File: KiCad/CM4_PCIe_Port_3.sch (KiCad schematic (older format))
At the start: 1 part, among them J15 10018783-10113TLF

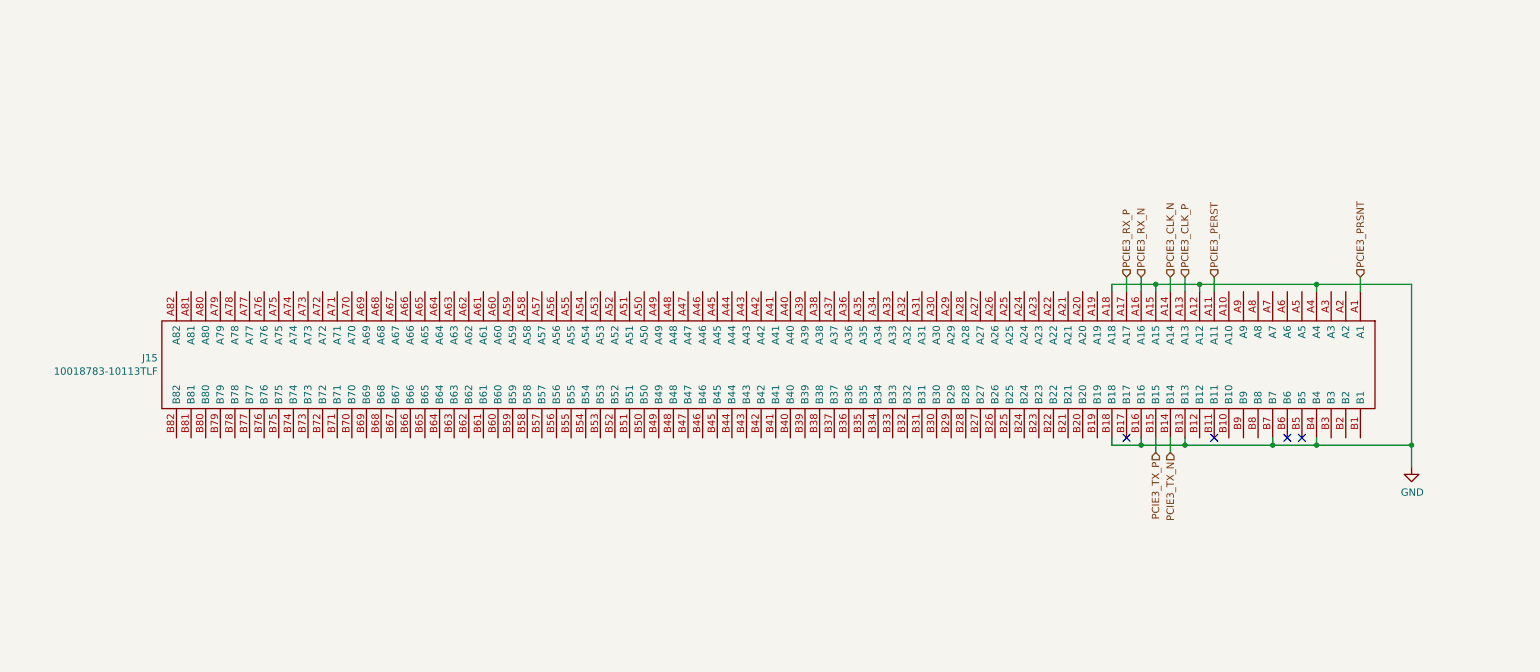
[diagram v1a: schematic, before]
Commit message: Updating PCIe symbols + PCIe power stub sheet
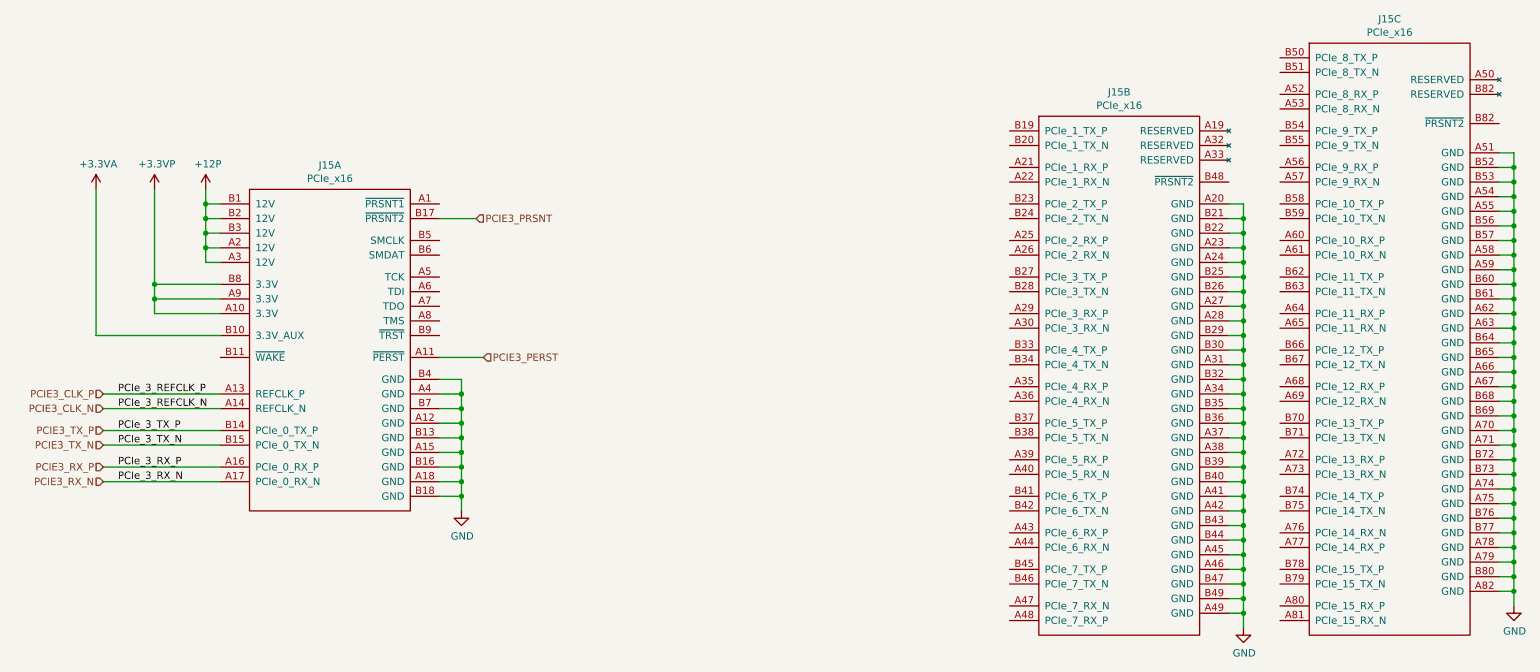
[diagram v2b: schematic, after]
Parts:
- removed J15: 10018783-10113TLF, 10018783-10113TLF, symbol CM4_MATX:10018783-10113TLF
- added J15: PCIe_x16, CM4_MATX:10018783-10113TLF, symbol CM4_MATX:PCIe_x16
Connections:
- net GND: now also J15.A12 (GND), J15.A15 (GND), J15.A18 (GND), J15.A20 (GND), J15.A23 (GND), J15.A24 (GND), J15.A27 (GND), J15.A28 (GND), J15.A31 (GND), J15.A34 (GND), J15.A37 (GND), J15.A38 (GND), J15.A4 (GND), J15.A41 (GND), J15.A42 (GND), J15.A45 (GND), J15.A46 (GND), J15.A49 (GND), J15.A51 (GND), J15.A54 (GND), J15.A55 (GND), J15.A58 (GND), J15.A59 (GND), J15.A62 (GND), J15.A63 (GND), J15.A66 (GND), J15.A67 (GND), J15.A70 (GND), J15.A71 (GND), J15.A74 (GND), J15.A75 (GND), J15.A78 (GND), J15.A79 (GND), J15.A82 (GND), J15.B13 (GND), J15.B16 (GND), J15.B18 (GND), J15.B21 (GND), J15.B22 (GND), J15.B25 (GND), J15.B26 (GND), J15.B29 (GND), J15.B30 (GND), J15.B32 (GND), J15.B35 (GND), J15.B36 (GND), J15.B39 (GND), J15.B4 (GND), J15.B40 (GND), J15.B43 (GND), J15.B44 (GND), J15.B47 (GND), J15.B49 (GND), J15.B52 (GND), J15.B53 (GND), J15.B56 (GND), J15.B57 (GND), J15.B60 (GND), J15.B61 (GND), J15.B64 (GND), J15.B65 (GND), J15.B68 (GND), J15.B69 (GND), J15.B7 (GND), J15.B72 (GND), J15.B73 (GND), J15.B76 (GND), J15.B77 (GND), J15.B80 (GND)
- net PCIE3_CLK_N: now also J15.A14 (REFCLK_N)
- net PCIE3_CLK_P: now also J15.A13 (REFCLK_P)
- net PCIE3_PERST: now also J15.A11 (~PERST)
- net PCIE3_PRSNT: now also J15.B17 (~PRSNT2)
- net PCIE3_RX_N: now also J15.A17 (PCIe_0_RX_N)
- net PCIE3_RX_P: now also J15.A16 (PCIe_0_RX_P)
- net PCIE3_TX_N: now also J15.B15 (PCIe_0_TX_N)
- net PCIE3_TX_P: now also J15.B14 (PCIe_0_TX_P)
- new net +12P: J15.A2 (12V), J15.A3 (12V), J15.B1 (12V), J15.B2 (12V), J15.B3 (12V)
- new net +3.3VA: J15.B10 (3.3V_AUX)
- new net +3.3VP: J15.A10 (3.3V), J15.A9 (3.3V), J15.B8 (3.3V)
- no-connect marks 4 -> 0
